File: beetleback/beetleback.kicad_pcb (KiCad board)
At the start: 2 copper layers, 20 x 26 mm, 12 parts, among them J1 Conn_01x01_Male, J2 Conn_01x03_Male, J3 Conn_01x01_Male, U1 TA6586, U2 ATtiny412-SS, U3 ME6214A33M3G

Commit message: beetle motor esc back
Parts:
- removed C3: 10uF, Capacitor_SMD:C_0805_2012Metric
- removed U3: ME6214A33M3G, Package_TO_SOT_SMD:SOT-23
- added C5: 22uF 18v, Capacitor_SMD:C_1206_3216Metric, F.Cu at (156.5, 123.0)
- added C6: 22uF 18v, Capacitor_SMD:C_1206_3216Metric, F.Cu at (156.5, 125.5)
- added C7: 22uF 18v, Capacitor_SMD:C_1206_3216Metric, F.Cu at (151.5, 123.0)
- added C8: 22uF 18v, Capacitor_SMD:C_1206_3216Metric, F.Cu at (151.5, 125.5)
- added C9: 1uF, Capacitor_SMD:C_0603_1608Metric, F.Cu at (156.0, 136.0)
- added J4: motor_pad_2, Connector_Pin:Pin_D1.3mm_L11.0mm, F.Cu at (142.0, 130.0)
- added R3: 1k 0.5W, Capacitor_SMD:C_0805_2012Metric, F.Cu at (149.4, 119.0)
- C1: value 10uF -> 2.2uF; footprint Capacitor_SMD:C_0805_2012Metric -> Capacitor_SMD:C_0603_1608Metric
- C2: value 100nF -> 2.2uF; footprint Capacitor_SMD:C_0805_2012Metric -> Capacitor_SMD:C_0603_1608Metric
- D1: value LED -> MM5Z5V1; footprint LED_SMD:LED_0603_1608Metric_Castellated -> Diode_SMD:D_SOD-523
- J1: value Conn_01x01_Male -> power in; footprint Connector_Wire:SolderWire-2sqmm_1x01_D2mm_OD3.9mm -> Connector_JST:JST_XA_B02B-XASK-1-A_1x02_P2.50mm_Vertical
- J2: value Conn_01x03_Male -> servo in
- J3: value Conn_01x01_Male -> motor_pad_1; footprint Connector_Wire:SolderWire-2sqmm_1x01_D2mm_OD3.9mm -> Connector_Pin:Pin_D1.3mm_L11.0mm
- R1, R2: value 330R -> 1k
- U1: value TA6586 -> ATtiny13A-SS; footprint Package_DIP:DIP-8_W7.62mm -> Package_SO:SOIC-8_3.9x4.9mm_P1.27mm
- U2: value ATtiny412-SS -> DRV8848; footprint Package_SO:SOIC-8_3.9x4.9mm_P1.27mm -> Package_SO:TSSOP-16-1EP_4.4x5mm_P0.65mm
- moved J1 17.7 mm to (154.5, 117.5)
- moved U1 11.7 mm to (143.0, 122.0), turned to 90 degrees
- moved D1 11.0 mm to (149.0, 121.0), turned to 0 degrees
- moved R2 9.72 mm to (146.5, 131.3), turned to -90 degrees
- moved C2 9.64 mm to (156.0, 134.0)
- moved R1 8.06 mm to (141.0, 116.5)
- moved C1 6.75 mm to (147.5, 122.5)
- moved J2 2.00 mm to (144.0, 116.0), turned to 90 degrees
- moved U2 0.69 mm to (150.0, 136.0)
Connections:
- C1 pad 1: VBAT -> +5V
- C2 pad 1: VLOGIC -> /DRV_VREF
- D1 pad 1: GND -> +5V
- D1 pad 2: Net-(D1-Pad2) -> GND
- J1 pad 1: /MOTORO1 -> /VBAT
- J2 pad 1: GND -> Net-(J2-Pad1)
- J2 pad 2: VBAT -> Net-(J2-Pad2)
- J2 pad 3: Net-(J2-Pad3) -> GND
- J3 pad 1: /MOTORO2 -> /MOTOR_PAD_1
- R1 pad 1: Net-(J2-Pad3) -> Net-(J2-Pad1)
- R1 pad 2: PWM -> /PWMIN
- R2 pad 1: BLINKY -> +5V
- R2 pad 2: Net-(D1-Pad2) -> /~SLEEP
- U1 pad 1: /MOTORB -> Net-(U1-Pad1)
- U1 pad 2: /MOTORF -> /~FAULT
- U1 pad 3: GND -> Net-(U1-Pad3)
- U1 pad 4: VBAT -> GND
- U1 pad 5: /MOTORO1 -> /MOTOR_PWM_2
- U1 pad 6: /MOTORO1 -> /MOTOR_PWM_1
- U1 pad 7: /MOTORO2 -> /PWMIN
- U1 pad 8: /MOTORO2 -> +5V
- U2 pad 1: VLOGIC -> /~SLEEP
- U2 pad 2: /MOTORF -> /MOTOR_PAD_1
- U2 pad 3: /MOTORB -> GND
- U2 pad 4: Net-(U2-Pad4) -> /MOTOR_PAD_2
- U2 pad 5: PWM -> /MOTOR_PAD_2
- U2 pad 6: Net-(U2-Pad6) -> GND
- U2 pad 7: BLINKY -> /MOTOR_PAD_1
- U2 pad 8: GND -> /~FAULT
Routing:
- net GND: track 21.8 -> 65.9 mm, vias 3 -> 10
- net VBAT: track 28.4 -> 0.00 mm
- net /MOTOR_PWM_1: track 0.00 -> 25.8 mm, vias 0 -> 2
- net /MOTORB: track 25.4 -> 0.00 mm, vias 1 -> 0
- net VLOGIC: track 25.0 -> 0.00 mm
- net /MOTOR_PWM_2: track 0.00 -> 24.1 mm, vias 0 -> 2
- net /MOTORF: track 23.8 -> 0.00 mm, vias 1 -> 0
- net /VBAT: track 0.00 -> 22.6 mm, vias 0 -> 5
- net PWM: track 21.6 -> 0.00 mm, vias 2 -> 0
- net /~FAULT: track 0.00 -> 20.7 mm, vias 0 -> 2
- net +5V: track 0.00 -> 20.4 mm
- net /MOTOR_PAD_1: track 0.00 -> 16.9 mm
- net /DRV_VREF: track 0.00 -> 11.2 mm
- net /MOTORO1: track 8.73 -> 0.00 mm
- net /MOTORO2: track 8.58 -> 0.00 mm
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- added copper zone on F.Cu, net /MOTOR_PAD_1
- added copper zone on F.Cu, net /MOTOR_PAD_2
- added copper zone on F.Cu, net /VBAT
- removed copper zone on F.Cu, net /MOTORO1
- removed copper zone on F.Cu, net /MOTORO2
- removed copper zone on F.Cu, net GND
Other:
- net class Default removed

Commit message: board update
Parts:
- added D2: Red LED, LED_SMD:LED_0603_1608Metric, F.Cu at (145.0, 128.0)
- added R4: 1k, Resistor_SMD:R_0603_1608Metric, F.Cu at (145.0, 126.5)
- C1, C2: value 2.2uF -> 2.2uF 25v
- C5, C6, C7, C8: value 22uF 18v -> 22uF 25v
- C9: value 1uF -> 2.2uF 25v
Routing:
- net Net-(U1-Pad3): track 0.00 -> 2.21 mm
- net Net-(D2-Pad2): track 0.00 -> 1.56 mm
- net GND: track 65.9 -> 67.0 mm, vias 10 -> 11

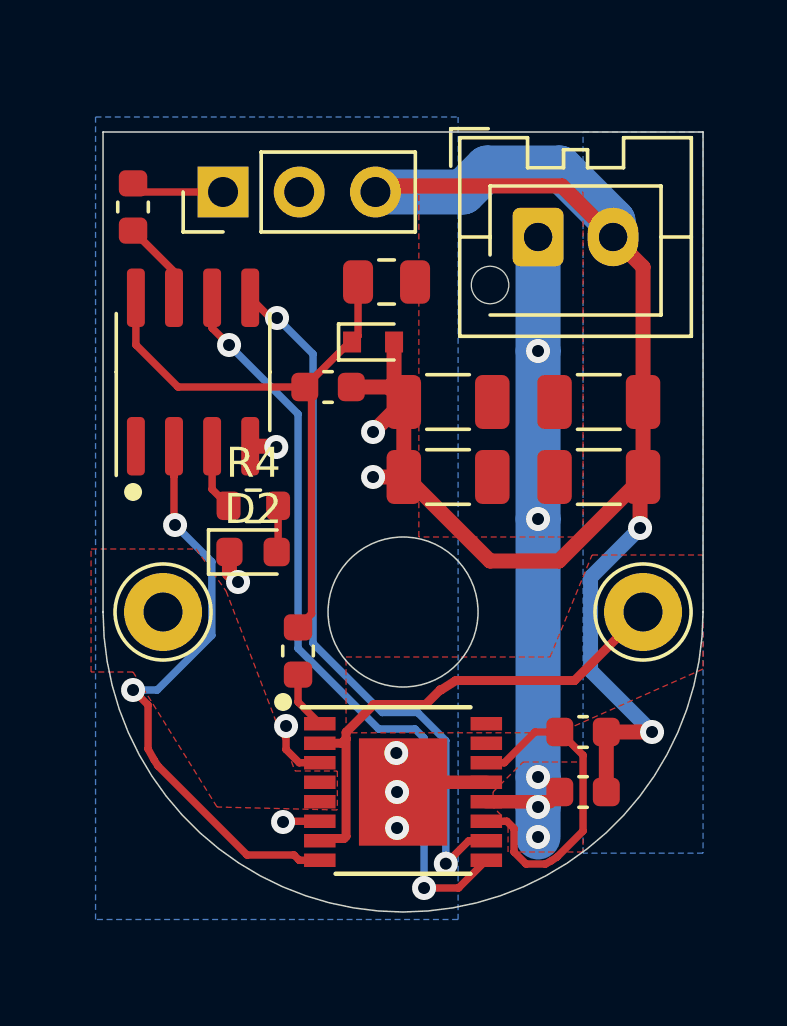
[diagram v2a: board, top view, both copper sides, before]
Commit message: Beetleweight motor back esc
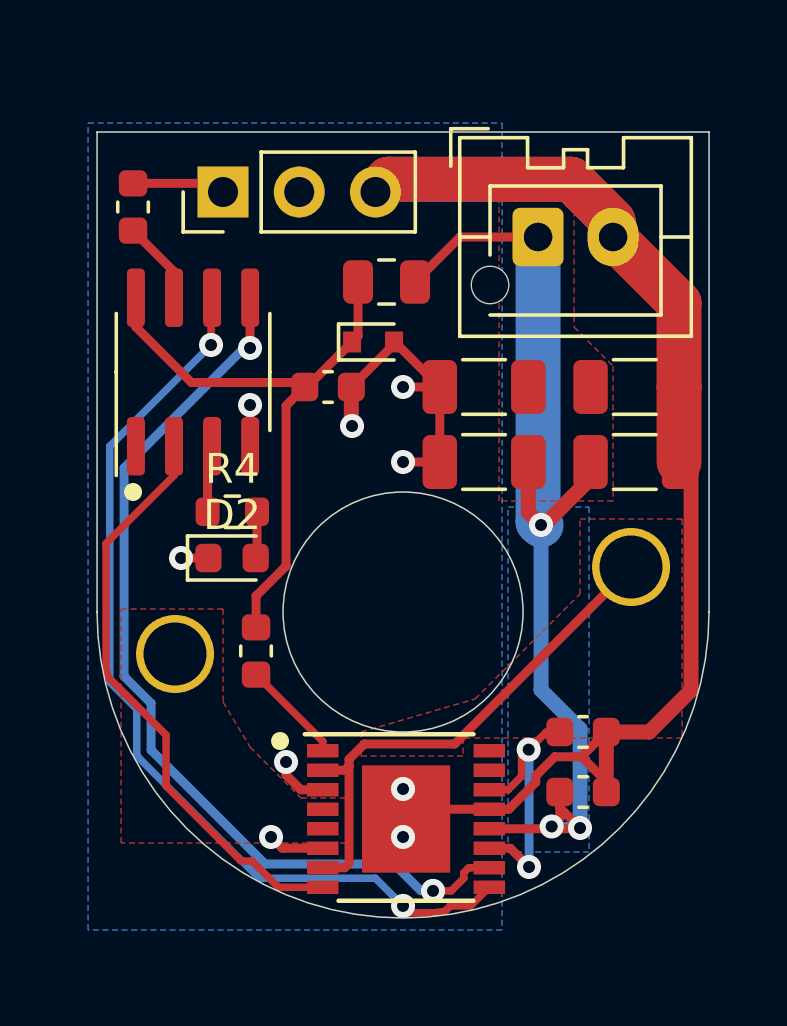
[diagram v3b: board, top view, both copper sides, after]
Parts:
- J3, J4: footprint Connector_Pin:Pin_D1.3mm_L11.0mm -> beetleback:bbb_motorpin
- moved J3 1.55 mm to (157.6, 128.5)
- moved J4 1.46 mm to (142.4, 131.4)
- moved R2 1.40 mm to (145.1, 131.3)
- moved C5 1.30 mm to (157.7, 122.5)
- moved C6 1.30 mm to (157.7, 125.0)
- moved C7 1.30 mm to (152.7, 122.5)
- moved C8 1.30 mm to (152.7, 125.0)
- moved U2 0.91 mm to (150.1, 136.9)
- moved R4 0.73 mm to (144.3, 126.7)
- moved D2 0.73 mm to (144.3, 128.2)
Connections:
- net Net-(J2-Pad2) renamed no_connect_15
- net Net-(U1-Pad1) renamed no_connect_16
- net Net-(U2-Pad15) renamed no_connect_17
- net Net-(U2-Pad16) renamed no_connect_18
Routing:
- net /VBAT: track 22.6 -> 36.9 mm, vias 5 -> 3
- net /MOTOR_PWM_2: track 24.1 -> 31.0 mm
- net /MOTOR_PWM_1: track 25.8 -> 31.3 mm
- net /DRV_VREF: track 11.2 -> 9.03 mm, vias 0 -> 2
- net GND: track 67.0 -> 65.2 mm, vias 11 -> 9
- net /~SLEEP: track 1.94 -> 3.46 mm
- net /~FAULT: track 20.7 -> 19.7 mm, vias 2 -> 0
- net /MOTOR_PAD_1: track 16.9 -> 17.4 mm
- added copper zone on B.Cu, net /VBAT
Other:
- board size 20 x 26 mm -> 20.4 x 26.2 mm

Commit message: Use double sided jst; add bbb logo
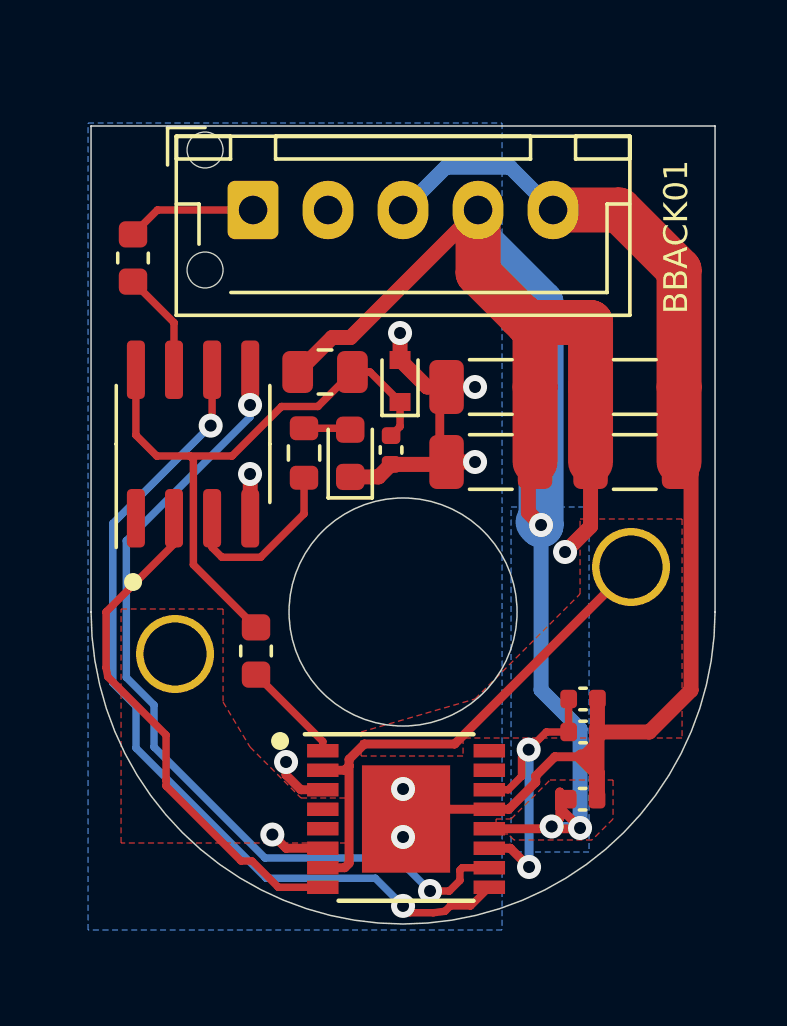
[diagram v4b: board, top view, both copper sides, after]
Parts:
- removed J2: servo in, Connector_PinHeader_2.54mm:PinHeader_1x03_P2.54mm_Vertical
- added C3: 1uF 25V, Capacitor_SMD:C_0402_1005Metric, F.Cu at (156.0, 132.9)
- added G***: LOGO, beetleback:bbb_logo, B.Cu at (156.4, 122.5)
- C1, C2, C9: value 2.2uF 25v -> 1uF 25V; footprint Capacitor_SMD:C_0603_1608Metric -> Capacitor_SMD:C_0402_1005Metric
- J1: value power in -> Conn_01x05_Female; footprint Connector_JST:JST_XA_B02B-XASK-1-A_1x02_P2.50mm_Vertical -> beetleback:JST_XH_B5B-XH-AM_doubleside
- R3: footprint Capacitor_SMD:C_0805_2012Metric -> Resistor_SMD:R_0805_2012Metric
- U2: value DRV8848 -> DRV8848PWPR
- moved J1 9.54 mm to (145.0, 116.6)
- moved D2 5.26 mm to (148.2, 124.7), turned to 90 degrees
- moved R3 3.63 mm to (147.4, 122.0), turned to 0 degrees
- moved R4 3.09 mm to (146.7, 124.7), turned to 90 degrees
- moved C1 2.97 mm to (149.6, 124.6), turned to -90 degrees
- moved U1 2.40 mm to (143.0, 124.4)
- moved R1 1.70 mm to (141.0, 118.2)
- moved D1 1.58 mm to (149.9, 122.3), turned to 90 degrees
- moved C9 0.24 mm to (156.0, 136.2)
- moved C7 0.23 mm to (152.9, 122.5)
- moved C8 0.23 mm to (152.9, 125.0)
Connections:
- J1 pad 1: /VBAT -> Net-(J1-Pad1)
- J1 pad 2: GND -> no_connect_15
- R1 pad 1: Net-(J2-Pad1) -> Net-(J1-Pad1)
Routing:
- net /VBAT: track 36.9 -> 59.7 mm, vias 3 -> 4
- net GND: track 65.2 -> 56.1 mm, vias 9 -> 8
- net Net-(J1-Pad1): track 0.00 -> 4.34 mm
- net /MOTOR_PWM_2: track 31.0 -> 27.2 mm
- net Net-(R4-Pad1): track 2.25 -> 5.98 mm
- net Net-(J2-Pad1): track 3.12 -> 0.00 mm
- net /MOTOR_PWM_1: track 31.3 -> 28.7 mm
- net /~FAULT: track 19.7 -> 17.3 mm
- net /DRV_VREF: track 9.03 -> 10.1 mm
- net /PWMIN: track 2.80 -> 3.50 mm
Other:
- board size 20.4 x 26.2 mm -> 20.8 x 26.6 mm
- board text added: "+"
- board text added: "-"
- board text added: "BBACK01"
- board text added: "RX GND"
- board text added: "RX IN"

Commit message: minor fixes
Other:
- board text added: "The jst connector can be fitted on either side. If fitted on the reverse, it must be flipped vertically so that the pinout is still correct."
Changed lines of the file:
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@@
     (effects (font (size 0.8 0.8) (thickness 0.15)))
+  )
+  (gr_text "The jst connector can be fitted on either side.\nIf fitted on the reverse, it must be flipped vertically so that the\npinout is still correct." (at 152 101.6) (layer "Dwgs.User")
+    (effects (font (size 1 1) (thickness 0.15)))
   )
   (dimension (type aligned) (layer "Dwgs.User")

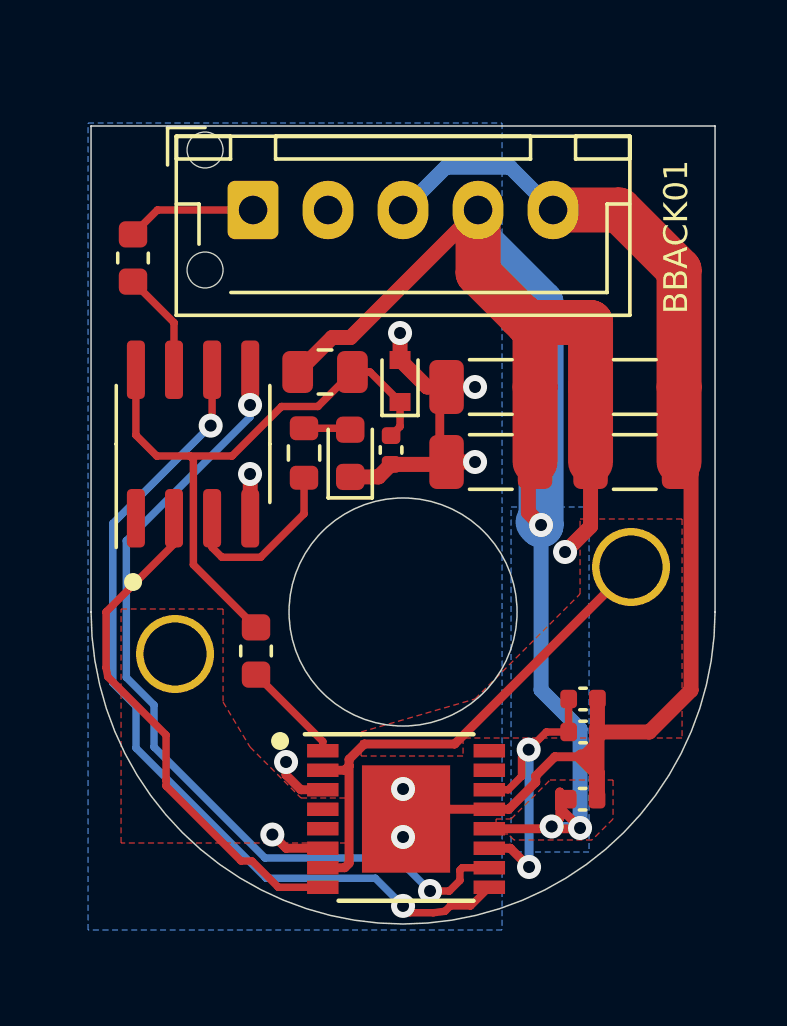
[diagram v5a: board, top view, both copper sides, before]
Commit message: Use 4-layer board
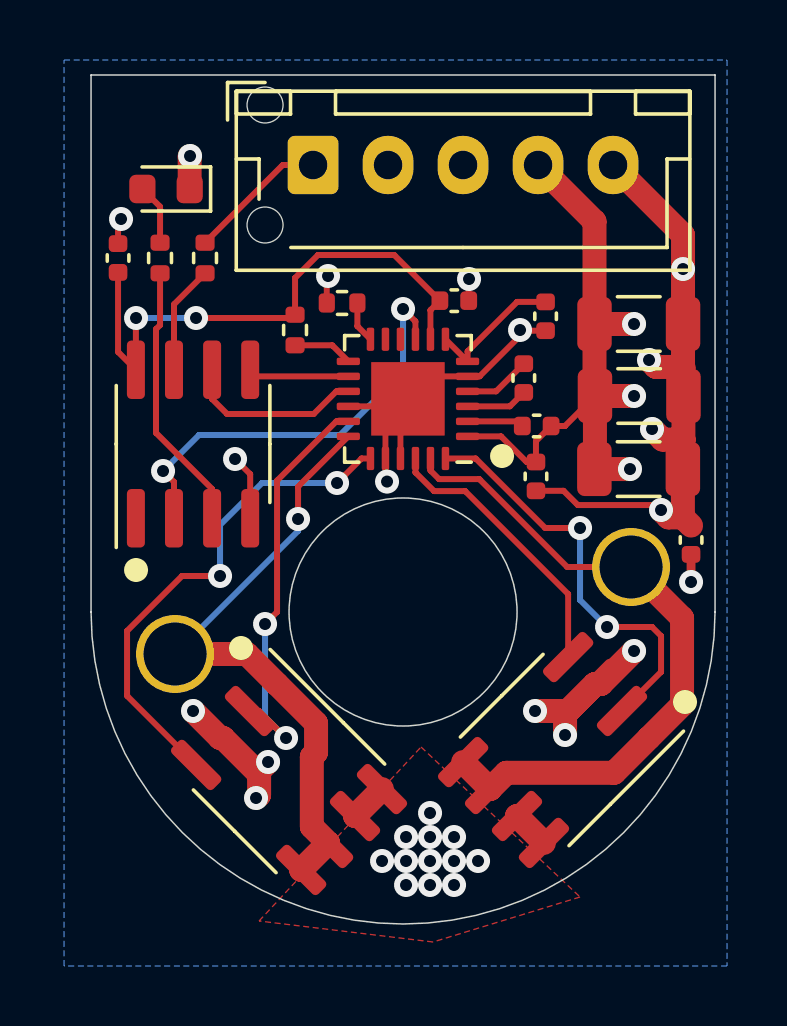
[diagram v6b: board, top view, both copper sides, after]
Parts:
- removed C8: 22uF 25v, Capacitor_SMD:C_1206_3216Metric
- removed D1: MM5Z5V1, Diode_SMD:D_SOD-523
- added C10: 1uF, Capacitor_SMD:C_0402_1005Metric, F.Cu at (151.7, 119.6)
- added C11: 1uF, Capacitor_SMD:C_0402_1005Metric, F.Cu at (154.8, 120.1)
- added C4: 0.1uF, Capacitor_SMD:C_0402_1005Metric, F.Cu at (154.0, 122.2)
- added Q1: IRF7351TRPBF, Package_SO:SOIC-8_3.9x4.9mm_P1.27mm, F.Cu at (146.2, 135.5)
- added Q2: IRF7351TRPBF, Package_SO:SOIC-8_3.9x4.9mm_P1.27mm, F.Cu at (155.1, 134.6)
- C2: value 1uF 25V -> 0.1uF
- C3: value 1uF 25V -> 1uF
- R1, R2, R4: footprint Resistor_SMD:R_0603_1608Metric -> Resistor_SMD:R_0402_1005Metric
- R3: value 1k 0.5W -> 33k TBC; footprint Resistor_SMD:R_0805_2012Metric -> Resistor_SMD:R_0402_1005Metric
- U2: value DRV8848PWPR -> DRV8701P; footprint Package_SO:TSSOP-16-1EP_4.4x5mm_P0.65mm -> Package_DFN_QFN:VQFN-24-1EP_4x4mm_P0.5mm_EP2.45x2.45mm
- moved U2 14.0 mm to (150.2, 122.9), turned to 180 degrees
- moved C1 11.1 mm to (140.5, 118.2), turned to 90 degrees
- moved R2 10.8 mm to (146.4, 120.6)
- moved D2 10.7 mm to (142.1, 115.9), turned to 180 degrees
- moved C9 9.37 mm to (159.6, 127.6), turned to 90 degrees
- moved C3 9.23 mm to (154.5, 123.8), turned to 180 degrees
- moved C2 8.66 mm to (154.4, 125.5), turned to -90 degrees
- moved R4 8.08 mm to (141.9, 118.2)
- moved C7 5.36 mm to (157.9, 120.4), turned to 0 degrees
- moved J1 2.50 mm to (147.0, 115.1)
- moved R1 2.40 mm to (143.4, 118.2)
- moved R3 2.37 mm to (148.0, 119.7), turned to 180 degrees
- moved C5 0.33 mm to (157.9, 122.8)
- moved C6 0.27 mm to (157.9, 125.2)
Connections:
- net no_connect_15 renamed no_connect_23
- net no_connect_16 renamed no_connect_24
- C1 pad 1: +5V -> +3V3
- C2 pad 1: /DRV_VREF -> /VBAT
- C3 pad 1: /DRV_VREF -> /VBAT
- C3 pad 2: GND -> Net-(C3-Pad2)
- R2 pad 1: +5V -> +3V3
- R2 pad 2: /~SLEEP -> Net-(R2-Pad2)
- R3 pad 1: /VBAT -> Net-(R3-Pad1)
- R3 pad 2: +5V -> GND
- U1 pad 8: +5V -> +3V3
- U2 pad 1: /~SLEEP -> /VBAT
- U2 pad 10: /MOTOR_PWM_2 -> no_connect_25
- U2 pad 11: /DRV_VREF -> no_connect_26
- U2 pad 12: /VBAT -> Net-(R3-Pad1)
- U2 pad 13: GND -> Net-(R2-Pad2)
- U2 pad 14: /DRV_VREF -> /MOTOR_PWM_2
- U2 pad 15: no_connect_17 -> /MOTOR_PWM_1
- U2 pad 16: no_connect_18 -> GND
- U2 pad 17: GND -> /GH1
- U2 pad 2: /MOTOR_PAD_1 -> Net-(C3-Pad2)
- U2 pad 3: GND -> Net-(C4-Pad1)
- U2 pad 4: /MOTOR_PAD_2 -> Net-(C4-Pad2)
- U2 pad 5: /MOTOR_PAD_2 -> GND
- U2 pad 6: GND -> /AVDD
- U2 pad 7: /MOTOR_PAD_1 -> /AVDD
- U2 pad 8: /~FAULT -> +3V3
- U2 pad 9: /MOTOR_PWM_1 -> /~FAULT
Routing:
- net /VBAT: track 59.7 -> 24.1 mm, vias 4 -> 16
- net /MOTOR_PWM_2: track 27.2 -> 3.36 mm, vias 2 -> 0
- net /MOTOR_PWM_1: track 28.7 -> 6.04 mm, vias 2 -> 0
- net /MOTOR_PAD_2: track 0.00 -> 20.8 mm, vias 0 -> 1
- net +5V: track 20.7 -> 0.00 mm
- net +3V3: track 0.00 -> 19.0 mm, vias 0 -> 2
- net /GL1: track 0.00 -> 16.9 mm, vias 0 -> 2
- net /GH2: track 0.00 -> 14.1 mm, vias 0 -> 2
- net /GH1: track 0.00 -> 13.8 mm, vias 0 -> 2
- net /DRV_VREF: track 10.1 -> 0.00 mm, vias 2 -> 0
- net /GL2: track 0.00 -> 9.33 mm
- net GND: track 56.1 -> 49.9 mm, vias 8 -> 17
- net /MOTOR_PAD_1: track 17.4 -> 22.5 mm
- net /AVDD: track 0.00 -> 4.66 mm
- net /~SLEEP: track 3.46 -> 0.00 mm
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- added copper zone on In1.Cu, net GND
- added copper zone on In2.Cu, net GND
- removed copper zone on F.Cu, net /MOTOR_PAD_1
- removed copper zone on F.Cu, net /MOTOR_PAD_2
- removed copper zone on B.Cu, net GND
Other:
- board size 20.8 x 26.6 mm -> 20.8 x 28.3 mm
- copper layers 2 -> 4
- board text added: "Leave space for test-clip on the ic"
- board text removed: "BBACK01"
